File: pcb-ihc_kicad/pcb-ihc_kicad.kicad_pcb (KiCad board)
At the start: 2 copper layers, 100 x 160 mm, 77 parts, among them J1 D-IN with pullup, J10 D-IN with pulldown, J11 2x N-Mosfet, J2 K1 - PD5, J3 K2 - PB7, J4 K3 - PB6, J5 K4 - PD4, J6 K5 - PD3, J7 K6 - PD2, J8 K7 - PD1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

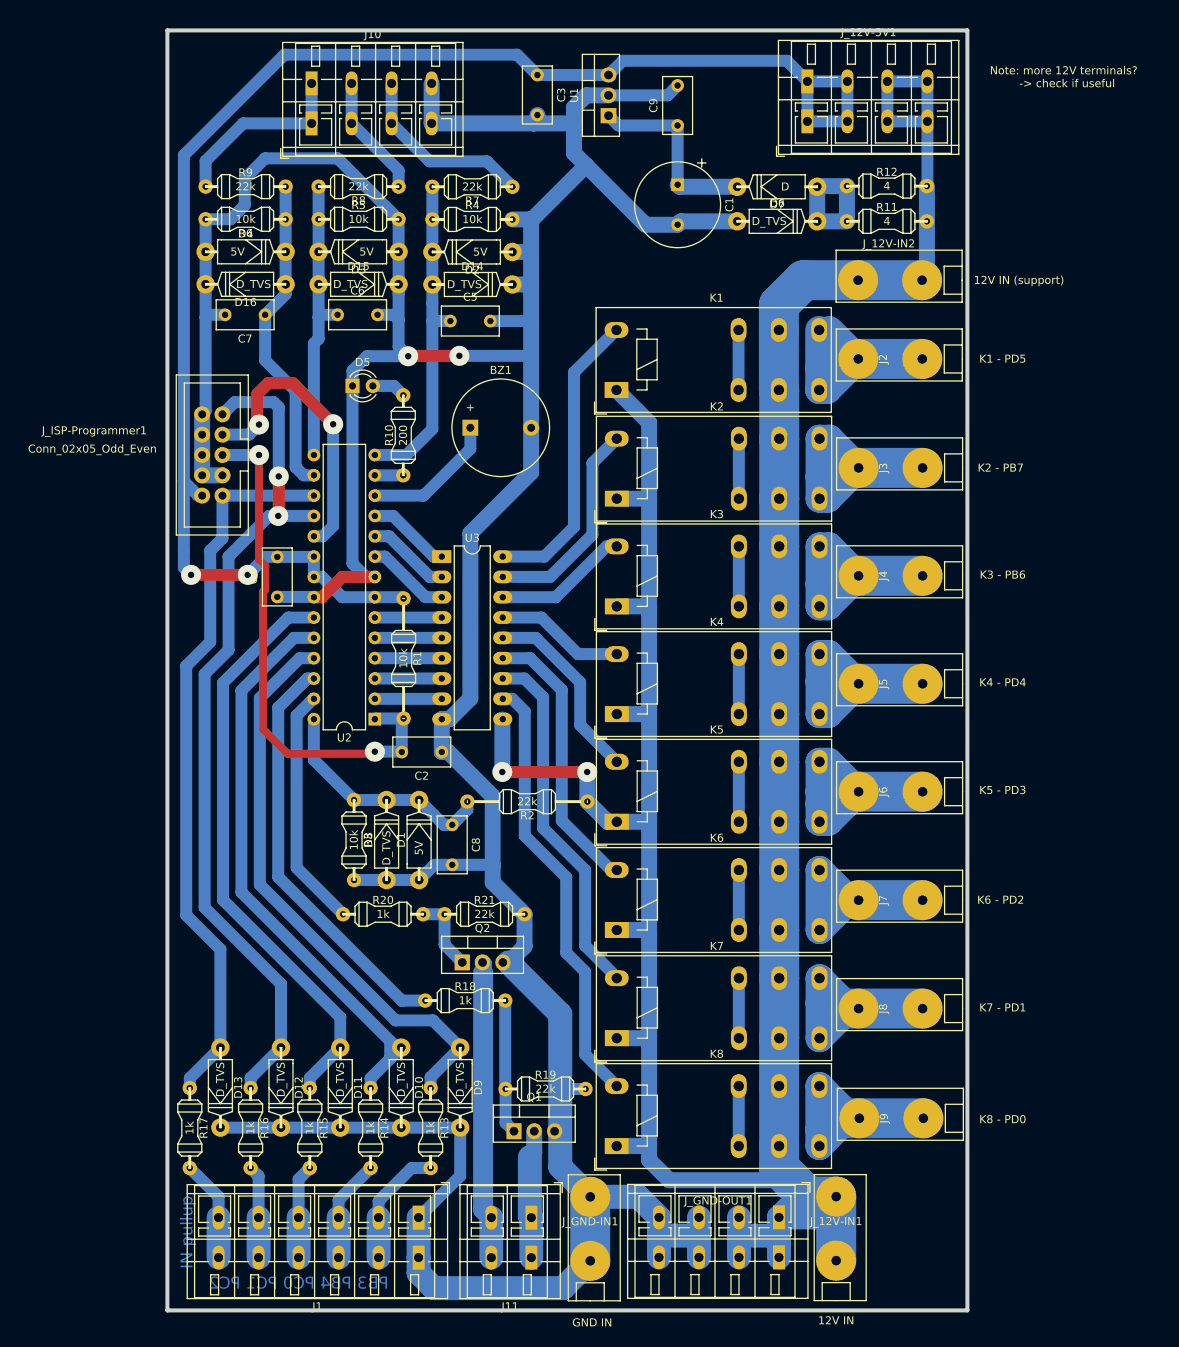
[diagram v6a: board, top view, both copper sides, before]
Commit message: Add text to copper back layer
Add description of terminals (desc, controller pin) as text to copper
layer. The plan is that the text is actually milled onto the pcb
(like tracks)
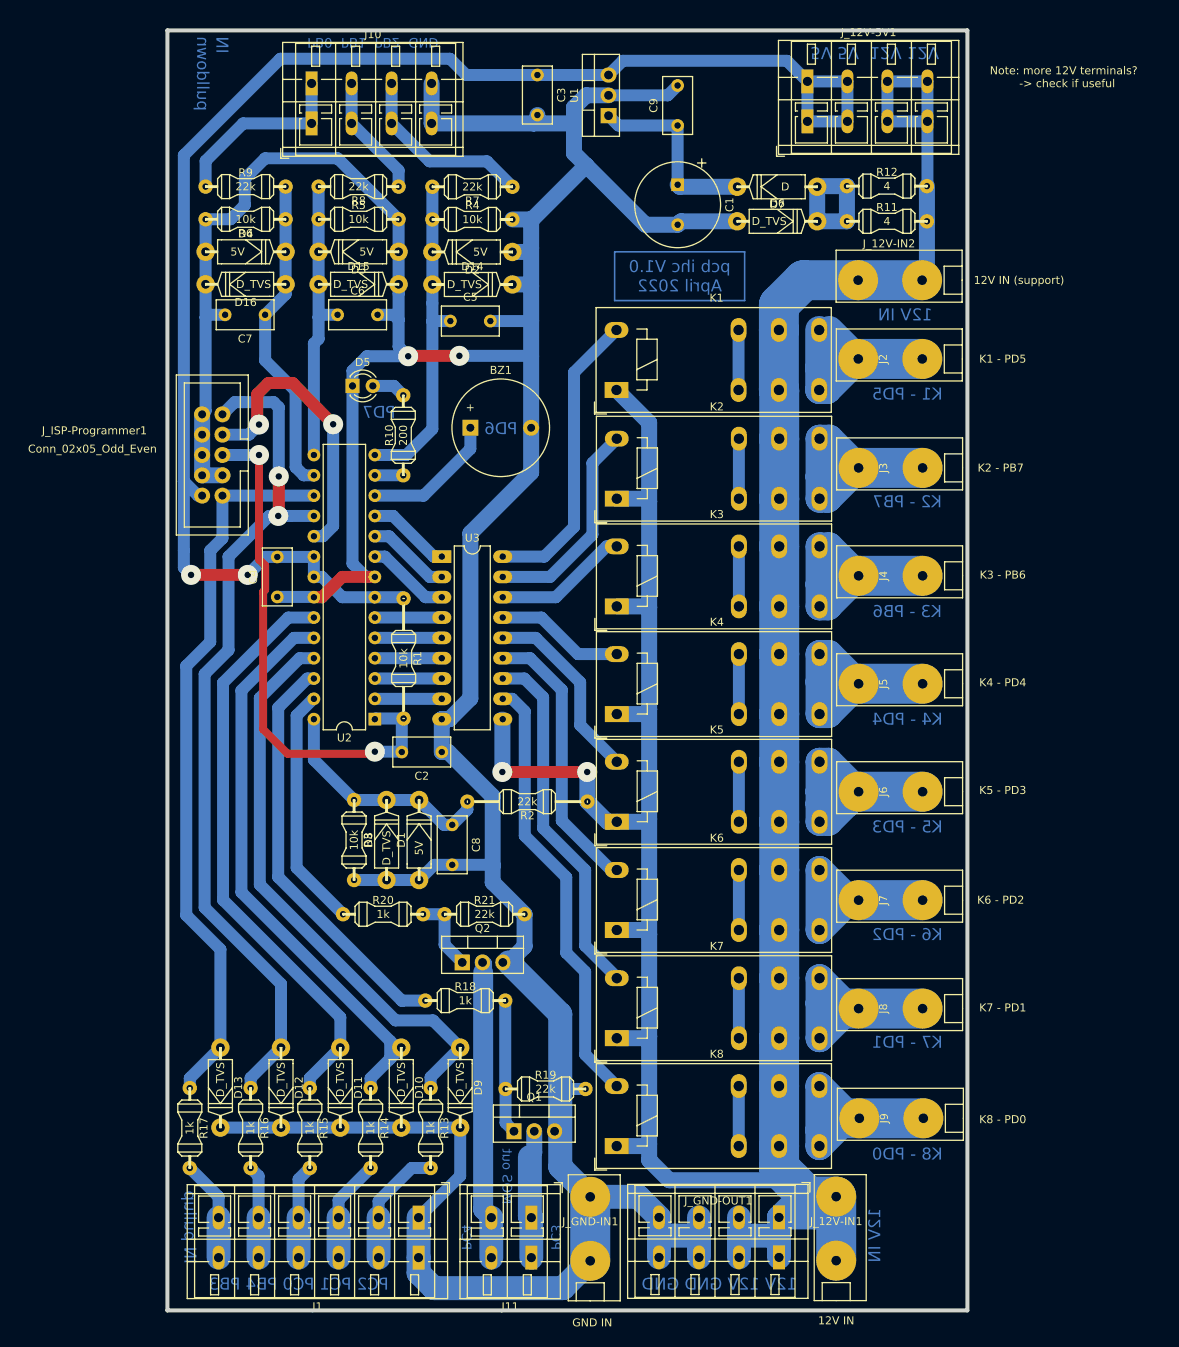
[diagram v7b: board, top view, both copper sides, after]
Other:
- board text added: "12V 12V GND GND"
- board text added: "12V IN"
- board text added: "5V 5V 12V 12V"
- board text added: "IN pulldown"
- board text added: "K1 - PD5"
- board text added: "K2 - PB7"
- board text added: "K3 - PB6"
- board text added: "K4 - PD4"
- board text added: "K5 - PD3"
- board text added: "K6 - PD2"
- board text added: "K7 - PD1"
- board text added: "K8 - PD0"
- board text added: "MOS out"
- board text added: "PB0 PB1 PB2 GND"
- board text added: "PC2 PC1 PC0 PB4 PB3"
- board text added: "PC3"
- board text added: "PC4"
- board text added: "PD6"
- board text added: "PD7"
- board text added: "pcb ihc V1.0 April 2022"
- board text removed: "PB3 PB4 PC0 PC1 PC2"
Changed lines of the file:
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@@
       (net 10 "Net-(J8-Pad1)") (pinfunction "Pin_1") (pintype "passive"))
   )
+  (gr_rect (start 120.904 42.672) (end 137.16 48.768) (layer "B.Cu") (width 0.2) (fill none))
   (gr_rect (start 165 15) (end 65 175) (layer "Edge.Cuts") (width 0.5) (fill none))
-  (gr_text "PB3 PB4 PC0 PC1 PC2" (at 81.407 171.577) (layer "B.Cu")
-    (effects (font (size 1.5 1.5) (thickness 0.1)) (justify mirror))
-  )
-  (gr_text "IN pullup" (at 67.437 165.227 90) (layer "B.Cu")
-    (effects (font (size 1.5 1.5) (thickness 0.3)))
+  (gr_text "IN \npulldown" (at 70.612 15.748 270) (layer "B.Cu")
+    (effects (font (size 1.5 1.5) (thickness 0.3)) (justify right mirror))
+  )
+  (gr_text "PC4" (at 102.362 165.862 270) (layer "B.Cu")
+    (effects (font (size 1.2 1.2) (thickness 0.2)) (justify mirror))
+  )
+  (gr_text "PC2 PC1 PC0 PB4 PB3" (at 81.407 171.704) (layer "B.Cu")
+    (effects (font (size 1.5 1.5) (thickness 0.3)) (justify mirror))
+  )
+  (gr_text "K1 - PD5" (at 157.48 60.452) (layer "B.Cu")
+    (effects (font (size 1.5 1.5) (thickness 0.3)) (justify mirror))
+  )
+  (gr_text "PD6" (at 106.68 64.77) (layer "B.Cu")
+    (effects (font (size 1.5 1.5) (thickness 0.3)) (justify mirror))
+  )
+  (gr_text "K8 - PD0" (at 157.48 155.448) (layer "B.Cu")
+    (effects (font (size 1.5 1.5) (thickness 0.3)) (justify mirror))
+  )
+  (gr_text "PD7" (at 91.44 62.738) (layer "B.Cu")
+    (effects (font (size 1.5 1.5) (thickness 0.3)) (justify mirror))
+  )
+  (gr_text "K3 - PB6" (at 157.48 87.63) (layer "B.Cu")
+    (effects (font (size 1.5 1.5) (thickness 0.3)) (justify mirror))
+  )
+  (gr_text "PB0  PB1  PB2  GND" (at 90.678 16.51 180) (layer "B.Cu")
+    (effects (font (size 1.2 1.2) (thickness 0.2)) (justify mirror))
+  )
+  (gr_text "IN pullup" (at 67.818 164.592 270) (layer "B.Cu")
+    (effects (font (size 1.5 1.5) (thickness 0.3)) (justify mirror))
+  )
+  (gr_text "pcb ihc V1.0\nApril 2022" (at 129.032 45.72) (layer "B.Cu")
+    (effects (font (size 1.5 1.5) (thickness 0.3)) (justify mirror))
+  )
+  (gr_text "K5 - PD3" (at 157.48 114.554) (layer "B.Cu")
+    (effects (font (size 1.5 1.5) (thickness 0.3)) (justify mirror))
+  )
+  (gr_text "5V 5V  12V 12V" (at 153.416 17.78 180) (layer "B.Cu")
+    (effects (font (size 1.5 1.5) (thickness 0.3)) (justify mirror))
+  )
+  (gr_text "12V 12V GND GND" (at 133.985 171.704) (layer "B.Cu")
+    (effects (font (size 1.5 1.5) (thickness 0.3)) (justify mirror))
+  )
+  (gr_text "12V IN" (at 153.416 165.608 90) (layer "B.Cu")
+    (effects (font (size 1.5 1.5) (thickness 0.3)) (justify mirror))
+  )
+  (gr_text "MOS out" (at 107.442 158.242 270) (layer "B.Cu")
+    (effects (font (size 1.2 1.2) (thickness 0.2)) (justify mirror))
+  )
+  (gr_text "PC3" (at 113.538 165.862 270) (layer "B.Cu")
+    (effects (font (size 1.2 1.2) (thickness 0.2)) (justify mirror))
+  )
+  (gr_text "12V IN" (at 157.226 50.546) (layer "B.Cu")
+    (effects (font (size 1.5 1.5) (thickness 0.3)) (justify mirror))
+  )
+  (gr_text "K7 - PD1" (at 157.48 141.478) (layer "B.Cu")
+    (effects (font (size 1.5 1.5) (thickness 0.3)) (justify mirror))
+  )
+  (gr_text "K4 - PD4" (at 157.48 101.092) (layer "B.Cu")
+    (effects (font (size 1.5 1.5) (thickness 0.3)) (justify mirror))
+  )
+  (gr_text "K2 - PB7" (at 157.48 73.914) (layer "B.Cu")
+    (effects (font (size 1.5 1.5) (thickness 0.3)) (justify mirror))
+  )
+  (gr_text "K6 - PD2" (at 157.48 128.016) (layer "B.Cu")
+    (effects (font (size 1.5 1.5) (thickness 0.3)) (justify mirror))
   )
   (gr_text "Note: more 12V terminals?\n  -> check if useful" (at 177.038 20.828) (layer "F.SilkS")
@@
   (segment (start 145.004 26.368) (end 150.004 26.368) (width 1.5) (layer "B.Cu") (net 3))
   (segment (start 78.74 80.812) (end 83.272 80.812) (width 1.5) (layer "B.Cu") (net 3))
-  (segment (start 67.056 30.607) (end 79.629 18.034) (width 1.5) (layer "B.Cu") (net 3))
   (segment (start 90.932 85.852) (end 94.371 85.852) (width 1.5) (layer "B.Cu") (net 3))
   (segment (start 111.252 20.574) (end 120.142 20.574) (width 1.5) (layer "B.Cu") (net 3))
+  (segment (start 102.362 20.574) (end 100.33 18.542) (width 1.5) (layer "B.Cu") (net 3))
+  (segment (start 67.056 30.607) (end 67.056 71.365869) (width 1.5) (layer "B.Cu") (net 3))
   (segment (start 120.142 20.574) (end 121.92 18.796) (width 1.5) (layer "B.Cu") (net 3))
+  (segment (start 111.252 20.574) (end 102.362 20.574) (width 1.5) (layer "B.Cu") (net 3))
+  (segment (start 100.33 18.542) (end 79.121 18.542) (width 1.5) (layer "B.Cu") (net 3))
   (segment (start 83.272 80.812) (end 83.312 80.772) (width 1.5) (layer "B.Cu") (net 3))
   (segment (start 75.0435 83.058) (end 77.2895 80.812) (width 1.5) (layer "B.Cu") (net 3))
@@
   (segment (start 67.056 71.365869) (end 67.056 80.01) (width 1.5) (layer "B.Cu") (net 3))
   (segment (start 94.371 85.852) (end 94.526 86.007) (width 1.5) (layer "B.Cu") (net 3))
-  (segment (start 67.056 71.365869) (end 67.056 30.607) (width 1.5) (layer "B.Cu") (net 3))
+  (segment (start 79.121 18.542) (end 67.056 30.607) (width 1.5) (layer "B.Cu") (net 3))
   (segment (start 67.056 82.1555) (end 67.9585 83.058) (width 1.5) (layer "B.Cu") (net 3))
   (segment (start 67.056 71.365869) (end 68.842131 73.152) (width 1.5) (layer "B.Cu") (net 3))
   (segment (start 83.312 80.772) (end 83.312 83.312) (width 1.5) (layer "B.Cu") (net 3))
-  (segment (start 108.712 18.034) (end 111.252 20.574) (width 1.5) (layer "B.Cu") (net 3))
   (segment (start 67.056 80.01) (end 67.056 82.1555) (width 1.5) (layer "B.Cu") (net 3))
   (segment (start 68.842131 73.152) (end 69.342 73.152) (width 1.5) (layer "B.Cu") (net 3))
-  (segment (start 79.629 18.034) (end 108.712 18.034) (width 1.5) (layer "B.Cu") (net 3))
   (segment (start 77.2895 80.812) (end 78.74 80.812) (width 1.5) (layer "B.Cu") (net 3))
   (segment (start 150.004 21.368) (end 145.004 21.368) (width 1.5) (layer "B.Cu") (net 3))
